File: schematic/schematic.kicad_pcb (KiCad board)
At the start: 4 copper layers, 44 x 112 mm, 6 parts, among them SW1 SW_Push

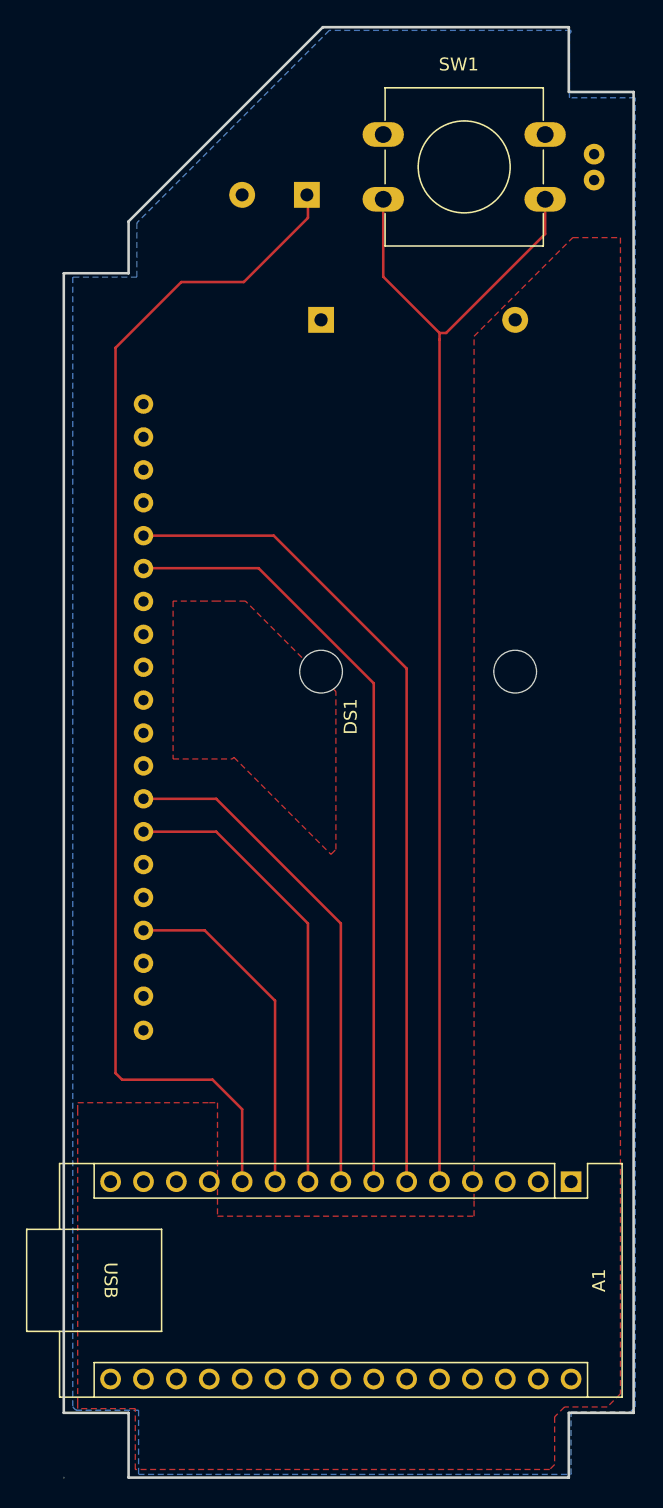
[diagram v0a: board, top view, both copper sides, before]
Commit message: fixed schematic edge cuts which was wrong by like 4mm
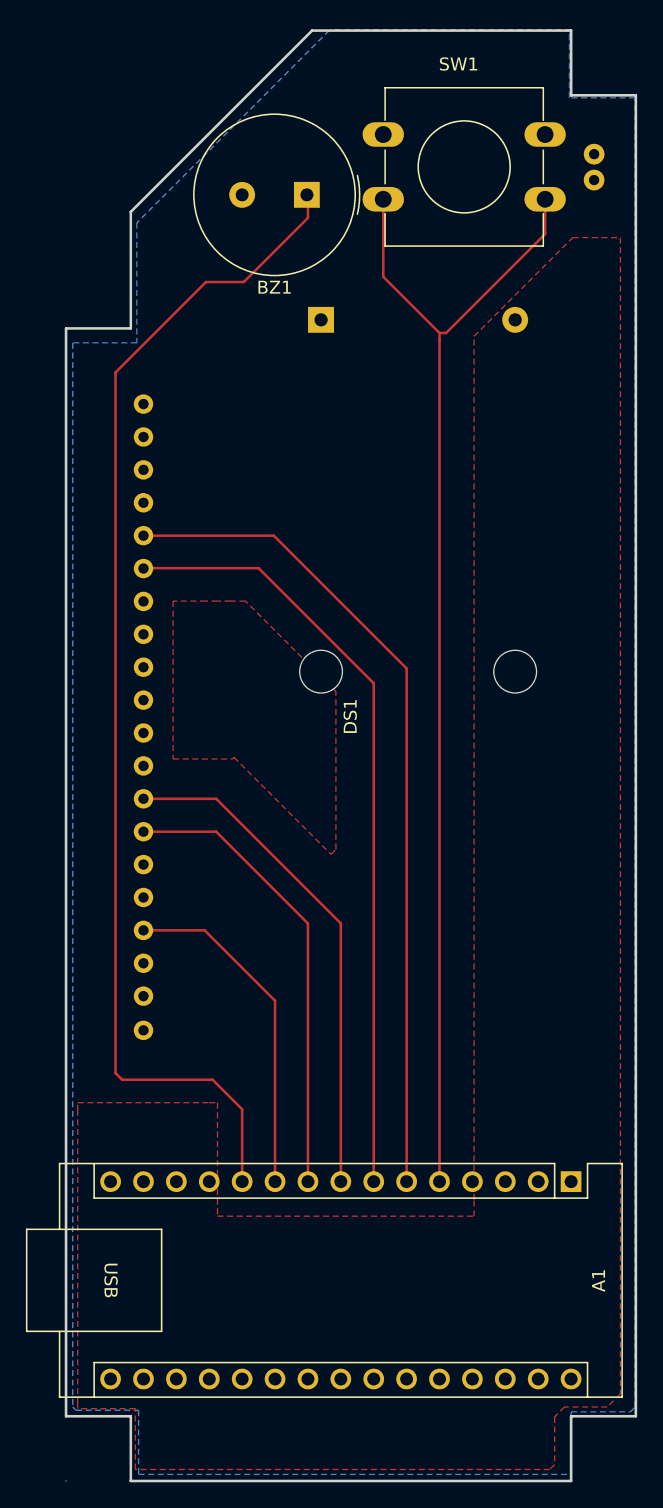
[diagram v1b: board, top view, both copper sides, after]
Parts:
- BZ1: moved to F.Cu
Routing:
- net Net-(A1-D8): track 93.4 -> 92.3 mm
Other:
- outline, holes or cut-outs redrawn
